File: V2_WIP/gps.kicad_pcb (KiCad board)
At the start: 6 copper layers, 82.5 x 82.5 mm, 62 parts, among them J4 BATT, J6 USB_B_Micro, J7 USB_B_Micro, SW1 RotaryEncoder_Switch, SW2 MSN22AFW01, U1 NEO-M9N, U10 24C32, U11 SN74LV1T34DBVRG4, U12 USBLC6-2SC6, U2 TPS613222ADBVR, U3 DFR0654, U4 HT16k33, U5 7seg_1x1_rgb, U6 7seg_1x1_rgb, U7 7seg_1x1_rgb, U8 KW4-804AGB, U9 TCA39306DDFR

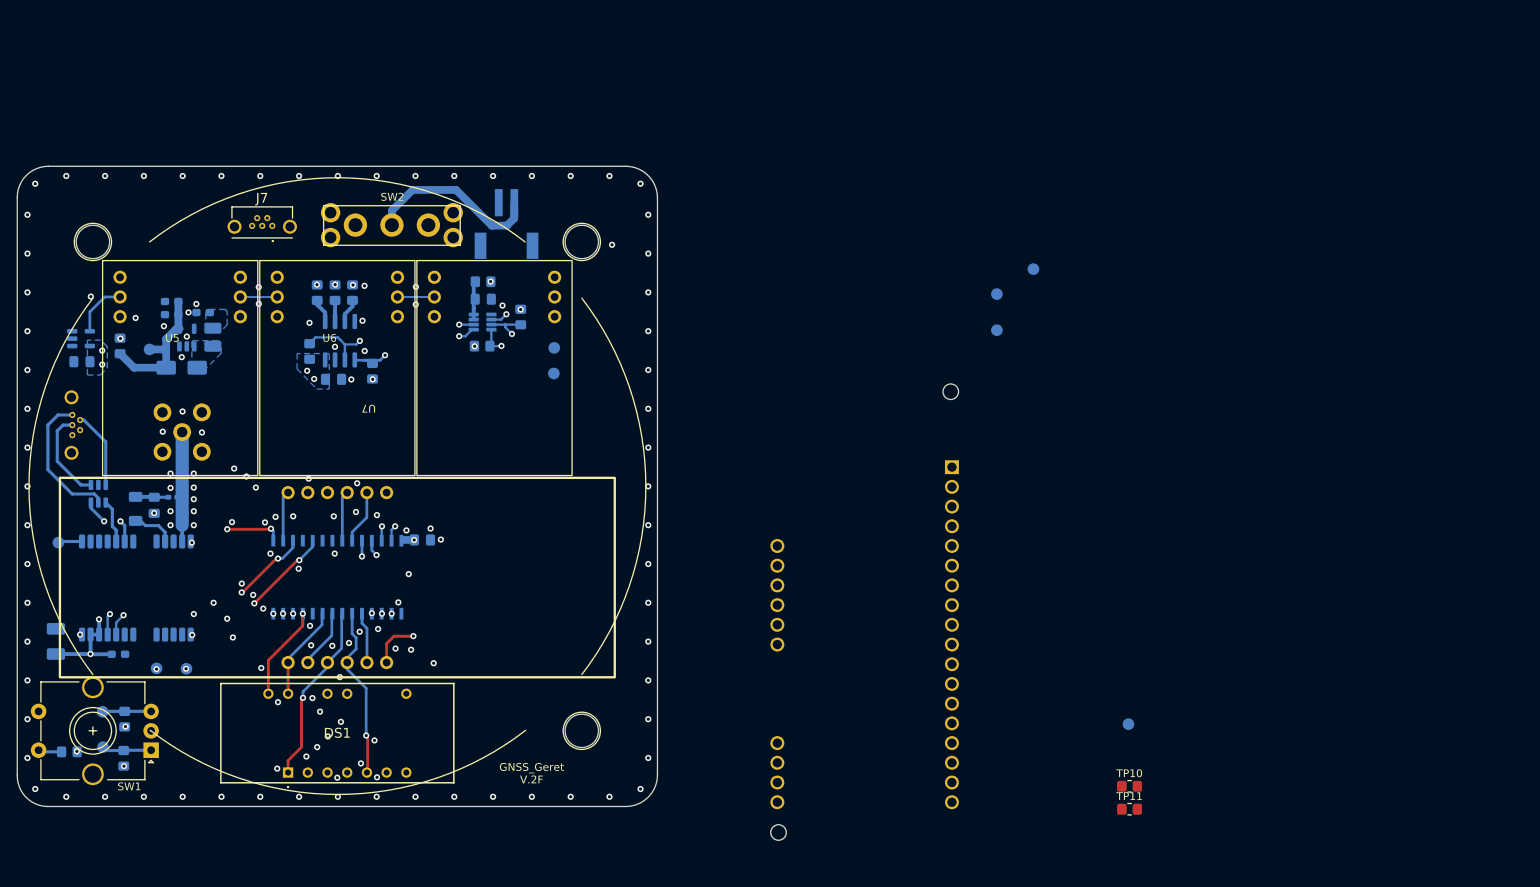
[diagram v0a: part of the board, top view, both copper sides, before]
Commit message: Cleaned schematic
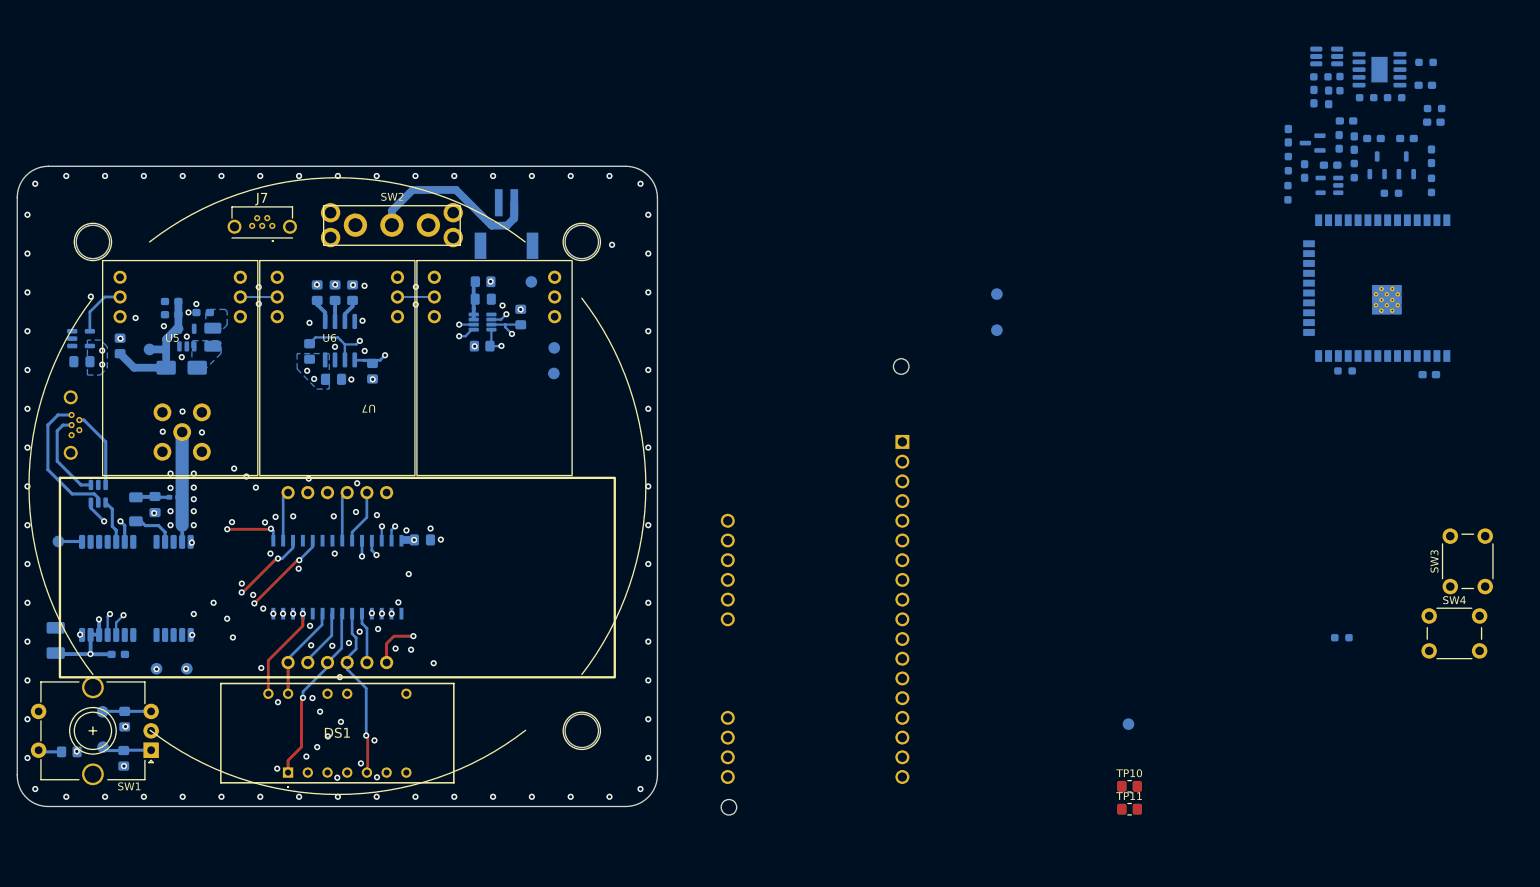
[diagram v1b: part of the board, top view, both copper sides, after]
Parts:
- removed AE1: Antenna_Shield, w_conn_rf:lemo_epb00250ntn
- removed J6: USB_B_Micro, KiCad:USB3145301A
- removed the L1 at (72.8, 84.4)
- removed TP14: SAFEBOOT_N, TestPoint:TestPoint_Pad_D1.5mm
- removed the TP4 at (74.5, 106.5)
- removed the TP5 at (70.7, 106.5)
- added AE401: Antenna_Shield, w_conn_rf:lemo_epb00250ntn, B.Cu at (74.0, 76.0)
- added C11: C, Capacitor_SMD:C_0603_1608Metric_Pad1.08x0.95mm_HandSolder, B.Cu at (225.0, 38.8)
- added C12: C, Capacitor_SMD:C_0603_1608Metric_Pad1.08x0.95mm_HandSolder, B.Cu at (216.5, 37.8)
- added C13: C, Capacitor_SMD:C_0603_1608Metric_Pad1.08x0.95mm_HandSolder, B.Cu at (219.8, 32.8)
- added C14: C, Capacitor_SMD:C_0603_1608Metric_Pad1.08x0.95mm_HandSolder, B.Cu at (224.0, 35.9)
- added C15: C, Capacitor_SMD:C_0603_1608Metric_Pad1.08x0.95mm_HandSolder, B.Cu at (234.2, 31.3)
- added C401: 10uF, Capacitor_Tantalum_SMD:CP_EIA-3528-15_AVX-H_Pad1.50x2.35mm_HandSolder, B.Cu at (57.7, 102.8)
- added C402: 1uF, Capacitor_SMD:C_0603_1608Metric_Pad1.08x0.95mm_HandSolder, B.Cu at (65.8, 104.7)
- added C403: 10n, Capacitor_SMD:C_0805_2012Metric_Pad1.18x1.45mm_HandSolder, B.Cu at (70.5, 85.3)
- added D1: LED, Diode_SMD:D_0603_1608Metric_Pad1.05x0.95mm_HandSolder, B.Cu at (235.0, 40.5)
- added D3: D, Diode_SMD:D_0603_1608Metric_Pad1.05x0.95mm_HandSolder, B.Cu at (223.1, 38.6)
- added D4: D, Diode_SMD:D_0603_1608Metric_Pad1.05x0.95mm_HandSolder, B.Cu at (218.6, 42.4)
- added D5: LED, Diode_SMD:D_0603_1608Metric_Pad1.05x0.95mm_HandSolder, B.Cu at (221.7, 32.9)
- added D6: D, Diode_SMD:D_0603_1608Metric_Pad1.05x0.95mm_HandSolder, B.Cu at (231.8, 38.2)
- added D7: D, Diode_SMD:D_0603_1608Metric_Pad1.05x0.95mm_HandSolder, B.Cu at (227.6, 38.2)
- added J301: USB_B_Micro, KiCad:USB3145301A, B.Cu at (60.0, 75.1)
- added L401: 27nH, Inductor_SMD:L_0402_1005Metric_Pad0.77x0.64mm_HandSolder, B.Cu at (72.9, 84.4)
- added Q1: IRLML5203, Package_TO_SOT_SMD:SOT-23, B.Cu at (219.7, 38.8)
- added Q2: S8050, Package_TO_SOT_SMD:SOT-23-3, B.Cu at (231.7, 41.6)
- added Q3: S8050, Package_TO_SOT_SMD:SOT-23-3, B.Cu at (228.0, 41.6)
- added R10: R, Resistor_SMD:R_0603_1608Metric_Pad0.98x0.95mm_HandSolder, B.Cu at (235.0, 44.2)
- added R11: R, Resistor_SMD:R_0603_1608Metric_Pad0.98x0.95mm_HandSolder, B.Cu at (225.0, 42.3)
- added R12: R, Resistor_SMD:R_0603_1608Metric_Pad0.98x0.95mm_HandSolder, B.Cu at (234.3, 28.4)
- added R13: R, Resistor_SMD:R_0603_1608Metric_Pad0.98x0.95mm_HandSolder, B.Cu at (223.2, 31.1)
- added R14: R, Resistor_SMD:R_0603_1608Metric_Pad0.98x0.95mm_HandSolder, B.Cu at (220.7, 30.2)
- added R15: R, Resistor_SMD:R_0603_1608Metric_Pad0.98x0.95mm_HandSolder, B.Cu at (226.6, 32.9)
- added R16: R, Resistor_SMD:R_0603_1608Metric_Pad0.98x0.95mm_HandSolder, B.Cu at (230.2, 32.9)
- added R20: R, Resistor_SMD:R_0603_1608Metric_Pad0.98x0.95mm_HandSolder, B.Cu at (229.8, 45.2)
- added R21: R, Resistor_SMD:R_0603_1608Metric_Pad0.98x0.95mm_HandSolder, B.Cu at (223.4, 102.5)
- added R401: 10, Resistor_SMD:R_1206_3216Metric_Pad1.30x1.75mm_HandSolder, B.Cu at (68.0, 86.0)
- added R7: R, Resistor_SMD:R_0603_1608Metric_Pad0.98x0.95mm_HandSolder, B.Cu at (216.5, 45.2)
- added R8: R, Resistor_SMD:R_0603_1608Metric_Pad0.98x0.95mm_HandSolder, B.Cu at (216.5, 41.4)
- added R9: R, Resistor_SMD:R_0603_1608Metric_Pad0.98x0.95mm_HandSolder, B.Cu at (235.4, 34.3)
- added SW3: SW_Push, Button_Switch_THT:SW_PUSH_6mm, F.Cu at (237.4, 95.9)
- added SW4: SW_Push, Button_Switch_THT:SW_PUSH_6mm, F.Cu at (234.7, 99.7)
- added TP301: SAFEBOOT_N, TestPoint:TestPoint_Pad_D1.5mm, B.Cu at (58.0, 90.1)
- added TP401: GNSS_TXD, TestPoint:TestPoint_Pad_D1.5mm, B.Cu at (74.6, 106.5)
- added TP402: GNSS_RXD, TestPoint:TestPoint_Pad_D1.5mm, B.Cu at (70.7, 106.5)
- added U13: TP4057, Package_TO_SOT_SMD:SOT-23-6_Handsoldering, B.Cu at (221.5, 27.6)
- added U14: CH340K, Package_SO:SSOP-10-1EP_3.9x4.9mm_P1mm_EP2.1x3.3mm, B.Cu at (228.3, 29.3)
- added U301: USBLC6-2SC6, Package_TO_SOT_SMD:SOT-23-6, B.Cu at (63.2, 84.0)
- added U401: NEO-M9N, RF_GPS:ublox_NEO, B.Cu at (68.1, 96.2)
- C1: value 10uF -> C; footprint Capacitor_Tantalum_SMD:CP_EIA-3528-15_AVX-H_Pad1.50x2.35mm_HandSolder -> Capacitor_SMD:C_0603_1608Metric_Pad1.08x0.95mm_HandSolder
- C2: value 1uF -> C
- C3: value 10n -> C; footprint Capacitor_SMD:C_0805_2012Metric_Pad1.18x1.45mm_HandSolder -> Capacitor_SMD:C_0603_1608Metric_Pad1.08x0.95mm_HandSolder
- R2: value 10 -> R; footprint Resistor_SMD:R_1206_3216Metric_Pad1.30x1.75mm_HandSolder -> Resistor_SMD:R_0603_1608Metric_Pad0.98x0.95mm_HandSolder
- U1: value NEO-M9N -> ESP32-WROOM-32E; footprint RF_GPS:ublox_NEO -> RF_Module:ESP32-WROOM-32D
- U12: value USBLC6-2SC6 -> RT9742AGJ5F; footprint Package_TO_SOT_SMD:SOT-23-6 -> Package_TO_SOT_SMD:TSOT-23-5
- moved C1 189.8 mm to (235.3, 36.1), turned to 0 degrees
- moved C2 168.5 mm to (222.0, 41.6), turned to 180 degrees
- moved U1 165.2 mm to (228.7, 57.5), turned to 90 degrees
- moved C3 165.2 mm to (234.7, 68.6), turned to 180 degrees
- moved U12 163.5 mm to (221.8, 44.2), turned to 180 degrees
- moved R2 156.9 mm to (223.9, 68.1), turned to 0 degrees
- moved TP7 64.7 mm to (119.0, 56.6)
- moved U3 7.17 mm to (155.3, 97.2)
- renumbered L2 to L1, TP8 to TP4, TP6 to TP5
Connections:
- net RGB_5V renamed Net-(U11-Y)
- net SW_BATT renamed Net-(J4-Pin_1)
- C1 pad 1: +3V3 -> /ESP/RST
- C3 pad 1: GND -> +3V3
- C3 pad 2: Net-(C3-Pad2) -> GND
- R2 pad 1: Net-(U1-VCC_RF) -> /ESP/IO27/D4
- R2 pad 2: Net-(C3-Pad2) -> Net-(R2-Pad2)
- R3 pad 1: +5V -> +3V3
- R3 pad 2: SDA_5V -> /SCL_ESP
- R4 pad 1: +5V -> +3V3
- R4 pad 2: SCL_5V -> /SDA_ESP
- R5 pad 1: +3V3 -> +5V
- R5 pad 2: SCL_3V3 -> /SDA_Display
- R6 pad 1: +3V3 -> +5V
- R6 pad 2: SDA_3V3 -> /SCL_Display
- SW2 pad 1: SW_ESP -> /VBATT
- TP1 pad 1: SDA_3V3 -> /SDA_ESP
- TP10 pad 2: RGB_3V3 -> /RGB
- TP11 pad 2: RGB_3V3 -> /RGB
- TP2 pad 1: SCL_3V3 -> /SCL_ESP
- TP3 pad 1: RGB_3V3 -> /RGB
- U1 pad 1: Net-(U1-~{SAFEBOOT}) -> GND
- U1 pad 10: GND -> /ESP/IO25/D2
- U1 pad 11: Net-(AE1-A) -> /ESP/IO26/D3
- U1 pad 12: GND -> /ESP/IO27/D4
- U1 pad 13: GND -> /ESP/IO14/D6
- U1 pad 14: unconnected-(U1-LNA_EN-Pad14) -> /ESP/IO12/D13
- U1 pad 15: unconnected-(U1-RESERVED-Pad15) -> GND
- U1 pad 16: unconnected-(U1-RESERVED-Pad16) -> /ESP/IO13/D7
- U1 pad 2: unconnected-(U1-D_SEL-Pad2) -> +3V3
- U1 pad 20: GNSS_TXD -> unconnected-(U1-NC-Pad20)
- U1 pad 21: GNSS_RXD -> unconnected-(U1-NC-Pad21)
- U1 pad 22: +3V3 -> unconnected-(U1-NC-Pad22)
- U1 pad 23: +3V3 -> /ESP/IO15/A4
- U1 pad 24: GND -> /ESP/IO2/D9
- U1 pad 3: PULSE -> /ESP/EN
- U1 pad 4: unconnected-(U1-EXTINT-Pad4) -> /ESP/IO36/A0
- U1 pad 5: Net-(U1-USB_DM) -> /ESP/IO39/A1
- U1 pad 6: Net-(U1-USB_DP) -> /ESP/IO34/A2
- U1 pad 7: unconnected-(U1-VDD_USB-Pad7) -> /ESP/IO35/A3
- U1 pad 9: Net-(U1-VCC_RF) -> unconnected-(U1-IO33-Pad9)
- U10 pad 5: SDA_5V -> /SDA_Display
- U10 pad 6: SCL_5V -> /SCL_Display
- U11 pad 2: RGB_3V3 -> /Display/RGB_3V3
- U12 pad 1: Net-(J6-D+) -> +3V3
- U12 pad 3: Net-(J6-D-) -> unconnected-(U12-~{FLG}-Pad3)
- U12 pad 4: Net-(U1-USB_DM) -> Net-(U12-EN)
- U12 pad 5: Net-(J6-VBUS) -> /ESP/VCC
- U3 pad 10: SDA_3V3 -> /SDA_ESP
- U3 pad 13: PULSE -> /Pulse
- U3 pad 19: GNSS_RXD -> /GNSS_RxD
- U3 pad 20: GNSS_TXD -> /GNSS_TxD
- U3 pad 28: SDA_3V3 -> /SDA_ESP
- U3 pad 29: SCL_3V3 -> /SCL_ESP
- U3 pad 9: SCL_3V3 -> /SCL_ESP
- U4 pad 26: SCL_5V -> /SCL_Display
- U4 pad 27: SDA_5V -> /SDA_Display
- U9 pad 3: SCL_3V3 -> /SCL_ESP
- U9 pad 4: SDA_3V3 -> /SDA_ESP
- U9 pad 5: SDA_5V -> /SDA_Display
- U9 pad 6: SCL_5V -> /SCL_Display
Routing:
- net (no net): track 0.00 -> 110.8 mm, vias 0 -> 8
- net SCL_5V: track 53.6 -> 0.00 mm, vias 3 -> 0
- net SDA_5V: track 47.5 -> 0.00 mm, vias 3 -> 0
- net Net-(J6-VBUS): track 18.0 -> 0.00 mm
- net Net-(J301-VBUS): track 0.00 -> 18.0 mm
- net Net-(AE401-A): track 0.00 -> 14.1 mm
- net Net-(AE1-A): track 14.1 -> 0.00 mm
- net Net-(J6-D+): track 11.8 -> 0.00 mm
- net Net-(J301-D+): track 0.00 -> 11.8 mm
- net Net-(J6-D-): track 10.0 -> 0.00 mm
- net Net-(J301-D-): track 0.00 -> 10.0 mm
- net Net-(U401-USB_DP): track 0.00 -> 8.04 mm, vias 0 -> 2
- net Net-(U1-USB_DP): track 8.04 -> 0.00 mm, vias 2 -> 0
- net Net-(U401-VCC_RF): track 0.00 -> 5.60 mm
- net Net-(U1-VCC_RF): track 5.60 -> 0.00 mm
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
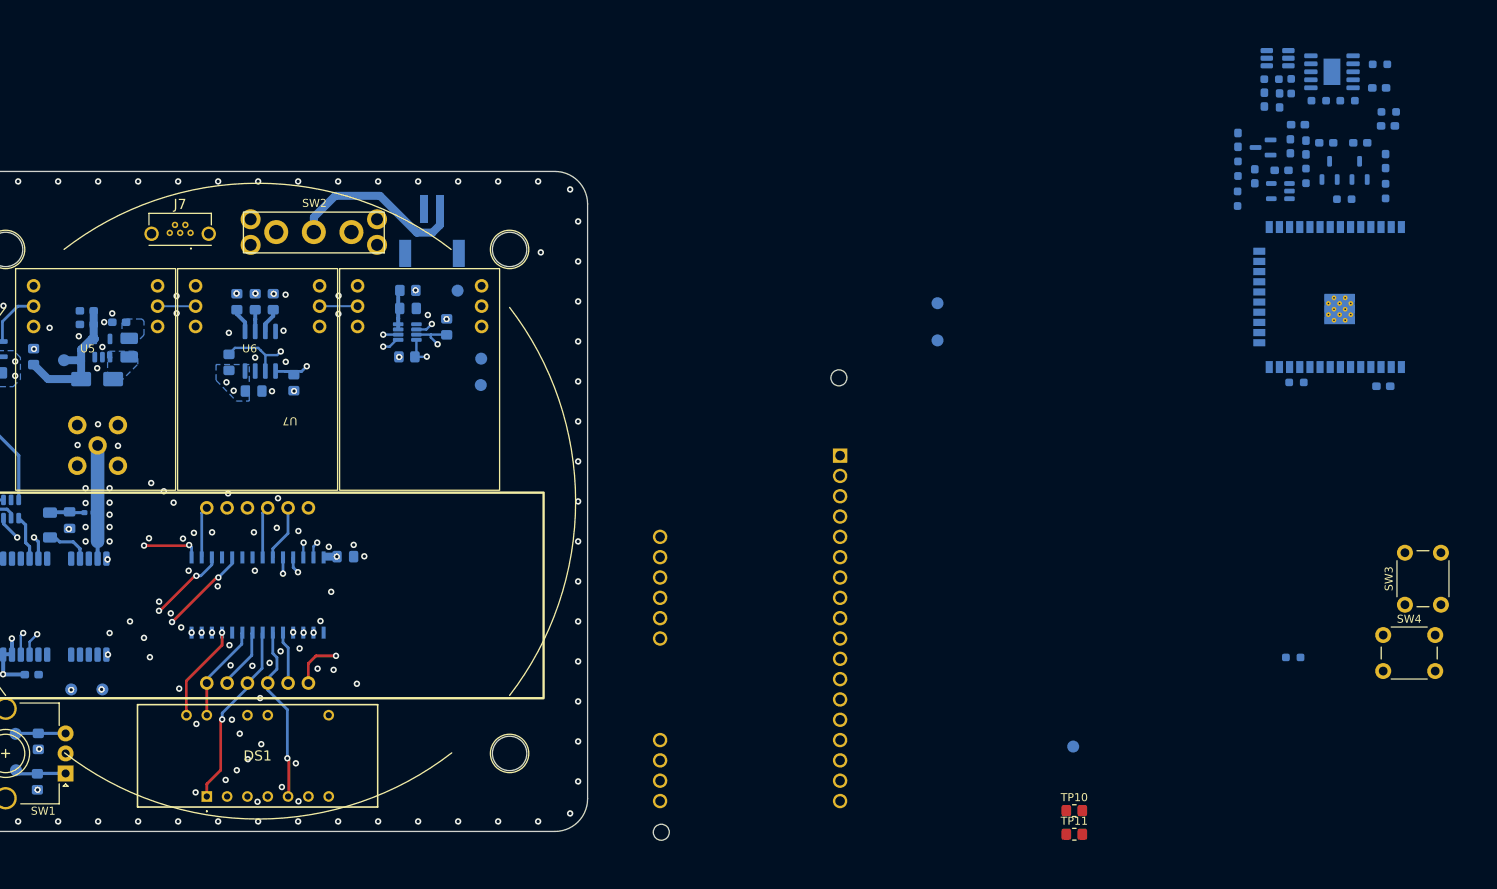
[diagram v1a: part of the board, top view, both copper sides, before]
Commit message: switched esp modul symbol for esp sheet
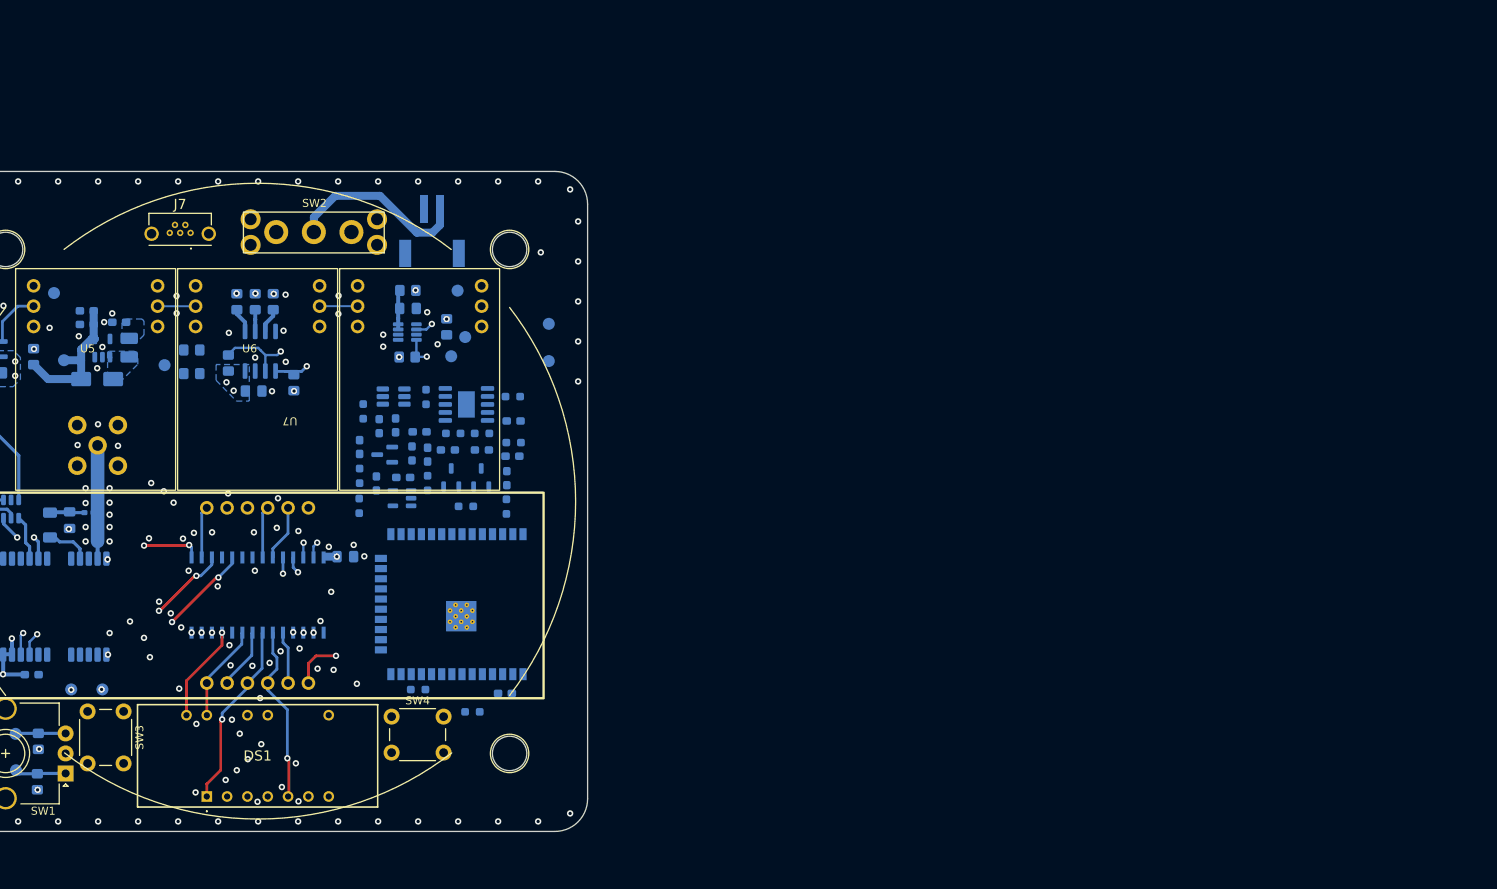
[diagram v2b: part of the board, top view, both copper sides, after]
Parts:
- removed U3: DFR0654, DFR0654:DFR0654_2
- added TP403: RGB_5V, TestPoint:TestPoint_Pad_D1.5mm, B.Cu at (68.5, 57.0)
- SW1: value RotaryEncoder_Switch -> RotaryEncoder
- TP10, TP11: moved to B.Cu
- TP3: value RGB_7seg -> RGB_3V3
- moved SW3 160.7 mm to (77.2, 109.2), turned to -90 degrees
- moved TP10 124.4 mm to (85.8, 64.1), turned to 180 degrees
- moved TP11 124.4 mm to (85.8, 67.0), turned to 180 degrees
- moved SW4 124.4 mm to (110.8, 109.9)
- moved TP3 123.2 mm to (82.4, 66.0)
- moved R14 120.9 mm to (107.2, 71.7), turned to -90 degrees
- moved D5 119.7 mm to (109.2, 73.6)
- moved U13 118.3 mm to (111.0, 69.9)
- moved C1 117.0 mm to (125.9, 77.3)
- moved R9 116.9 mm to (126.0, 75.6)
- moved D1 116.8 mm to (125.2, 80.1)
- moved R10 116.8 mm to (125.1, 83.6)
- moved C3 116.3 mm to (124.9, 107.0)
- moved Q1 116.3 mm to (109.9, 77.2)
- moved Q2 116.3 mm to (122.0, 80.0)
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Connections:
- net /Display/CC1 renamed /Display/DPX
- net /SCL_Display renamed /Display/SCL_5V
- net /SDA_Display renamed /Display/SDA_5V
- C11 pad 1: /ESP/VCC -> VCC
- D3 pad 1: /ESP/VCC -> VCC
- D4 pad 1: /ESP/VCC -> VCC
- Q1 pad 2: /ESP/VCC -> VCC
- R11 pad 1: /ESP/VCC -> VCC
- R3 pad 2: /SCL_ESP -> /ESP/IO22/SCL
- R4 pad 2: /SDA_ESP -> /ESP/IO21/SDA
- R_E1 pad 1: DT -> /DT
- R_E2 pad 1: CLK -> /CLK
- R_E3 pad 1: SW -> /SW
- SW1 pad A: CLK -> /CLK
- SW1 pad B: DT -> /DT
- SW1 pad S1: SW -> /SW
- TP10 pad 1: Net-(U3-MOSI) -> /ESP/IO23/MOSI
- TP11 pad 1: Net-(U3-D7) -> /ESP/IO13/D7
- TP12 pad 1: Net-(U3-D13) -> /ESP/IO12/D13
- TP13 pad 1: Net-(U3-D12) -> /ESP/IO4/D12
- TP4 pad 1: DT -> /DT
- TP401 pad 1: GNSS_TXD -> /GNSS_TxD
- TP402 pad 1: GNSS_RXD -> /GNSS_RxD
- TP9 pad 1: CLK -> /CLK
- U1 pad 10: /ESP/IO25/D2 -> /CLK
- U1 pad 11: /ESP/IO26/D3 -> /SW
- U1 pad 13: /ESP/IO14/D6 -> /Pulse
- U1 pad 23: /ESP/IO15/A4 -> /DT
- U1 pad 27: /ESP/IO16/D11 -> /GNSS_TxD
- U1 pad 28: /ESP/IO17/D10 -> /GNSS_RxD
- U11 pad 2: /Display/RGB_3V3 -> /RGB
- U12 pad 5: /ESP/VCC -> VCC
- U9 pad 3: /SCL_ESP -> /ESP/IO22/SCL
- U9 pad 4: /SDA_ESP -> /ESP/IO21/SDA
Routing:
- net (no net): track 110.8 -> 45.3 mm, vias 8 -> 3
- net /Display/SCL_5V: track 0.00 -> 51.8 mm, vias 0 -> 3
- net GNSS_TXD: track 13.8 -> 0.00 mm, vias 2 -> 0
- net /GNSS_TxD: track 0.00 -> 13.8 mm, vias 0 -> 2
- net GNSS_RXD: track 12.4 -> 0.00 mm, vias 2 -> 0
- net /GNSS_RxD: track 0.00 -> 12.4 mm, vias 0 -> 2
- net CLK: track 6.40 -> 0.00 mm
- net /CLK: track 0.00 -> 6.40 mm
- net DT: track 6.28 -> 0.00 mm
- net /DT: track 0.00 -> 6.28 mm
- net /ESP/IO21/SDA: track 0.00 -> 4.30 mm, vias 0 -> 1
- net SW: track 3.05 -> 0.00 mm
- net /SW: track 0.00 -> 3.05 mm
- net +3V3: track 132.5 -> 130.5 mm, vias 9 -> 8
- net /Display/SDA_5V: track 0.00 -> 0.26 mm, vias 0 -> 1
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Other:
- outline, holes or cut-outs redrawn
- board text removed: "D+"
- board text removed: "D-"
- board text removed: "VBUS"
